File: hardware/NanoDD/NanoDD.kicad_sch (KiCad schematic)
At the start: 33 parts, among them J1 Screw_Terminal_01x02, J2 Conn_01x06, J3 Screw_Terminal_01x02, Q1 AO3401A, Q2 AO3401A, U1 MSP430G2452IRSA16, U3 ZD24C128A-XGMB, U4 XC6206PxxxMR, U5 MS5607-02BA

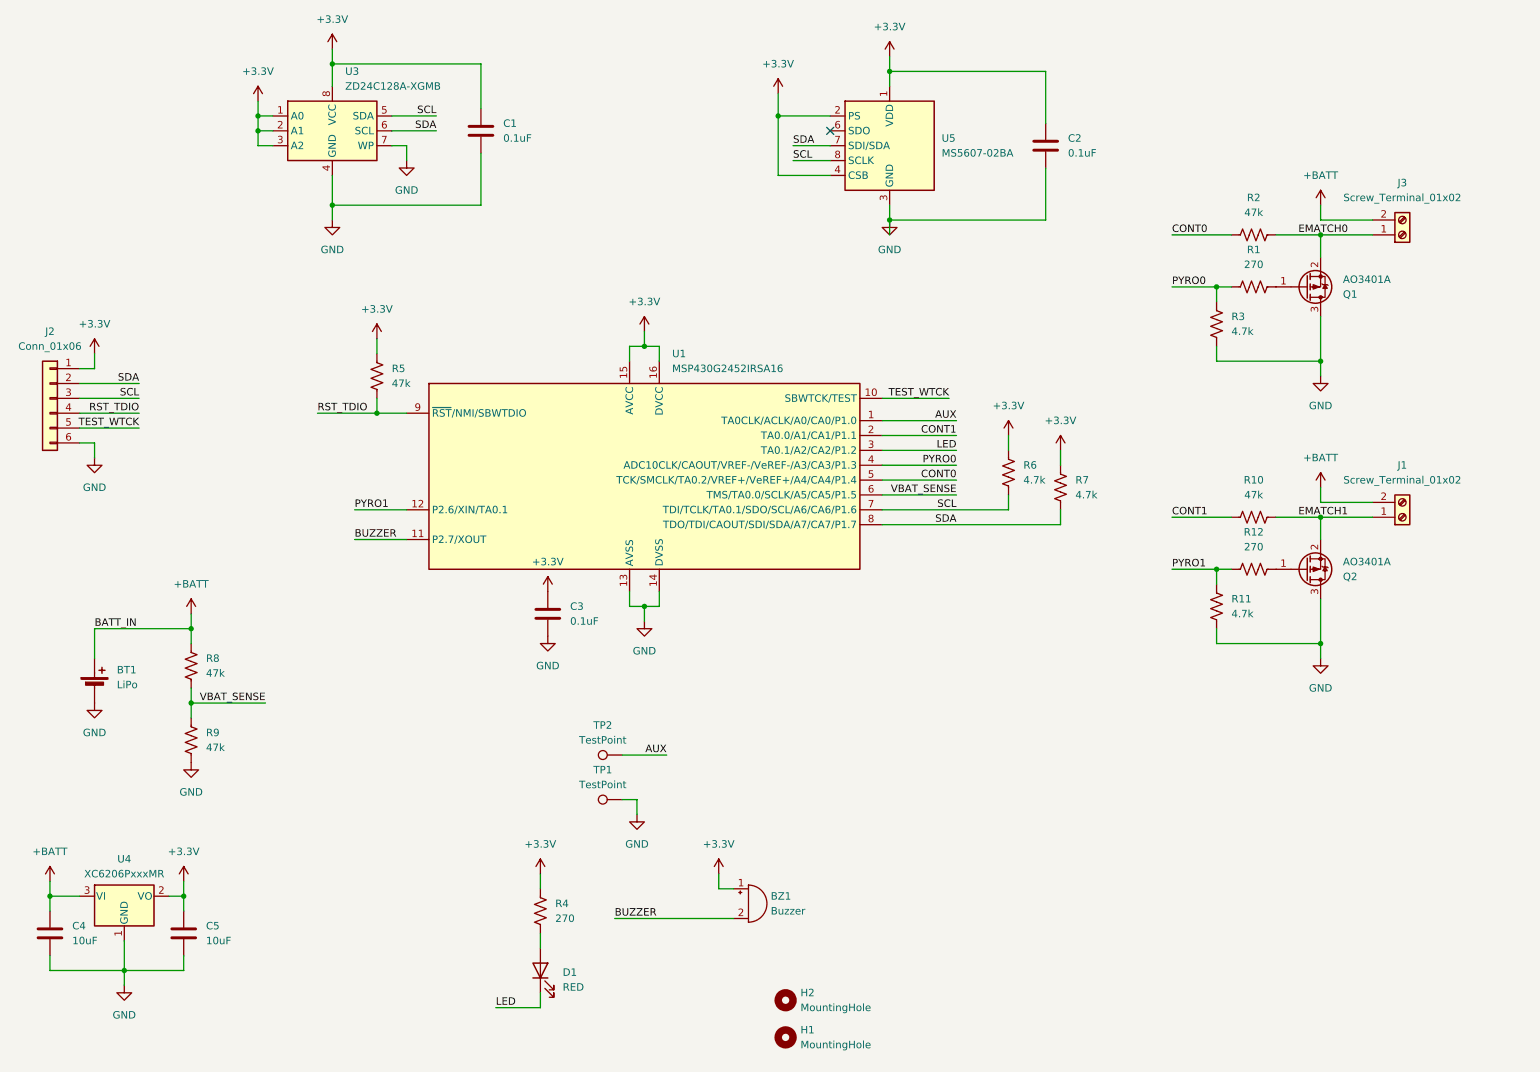
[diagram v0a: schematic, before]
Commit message: Even more layout shrink, switch to barometer that's cheap on JLCPCB
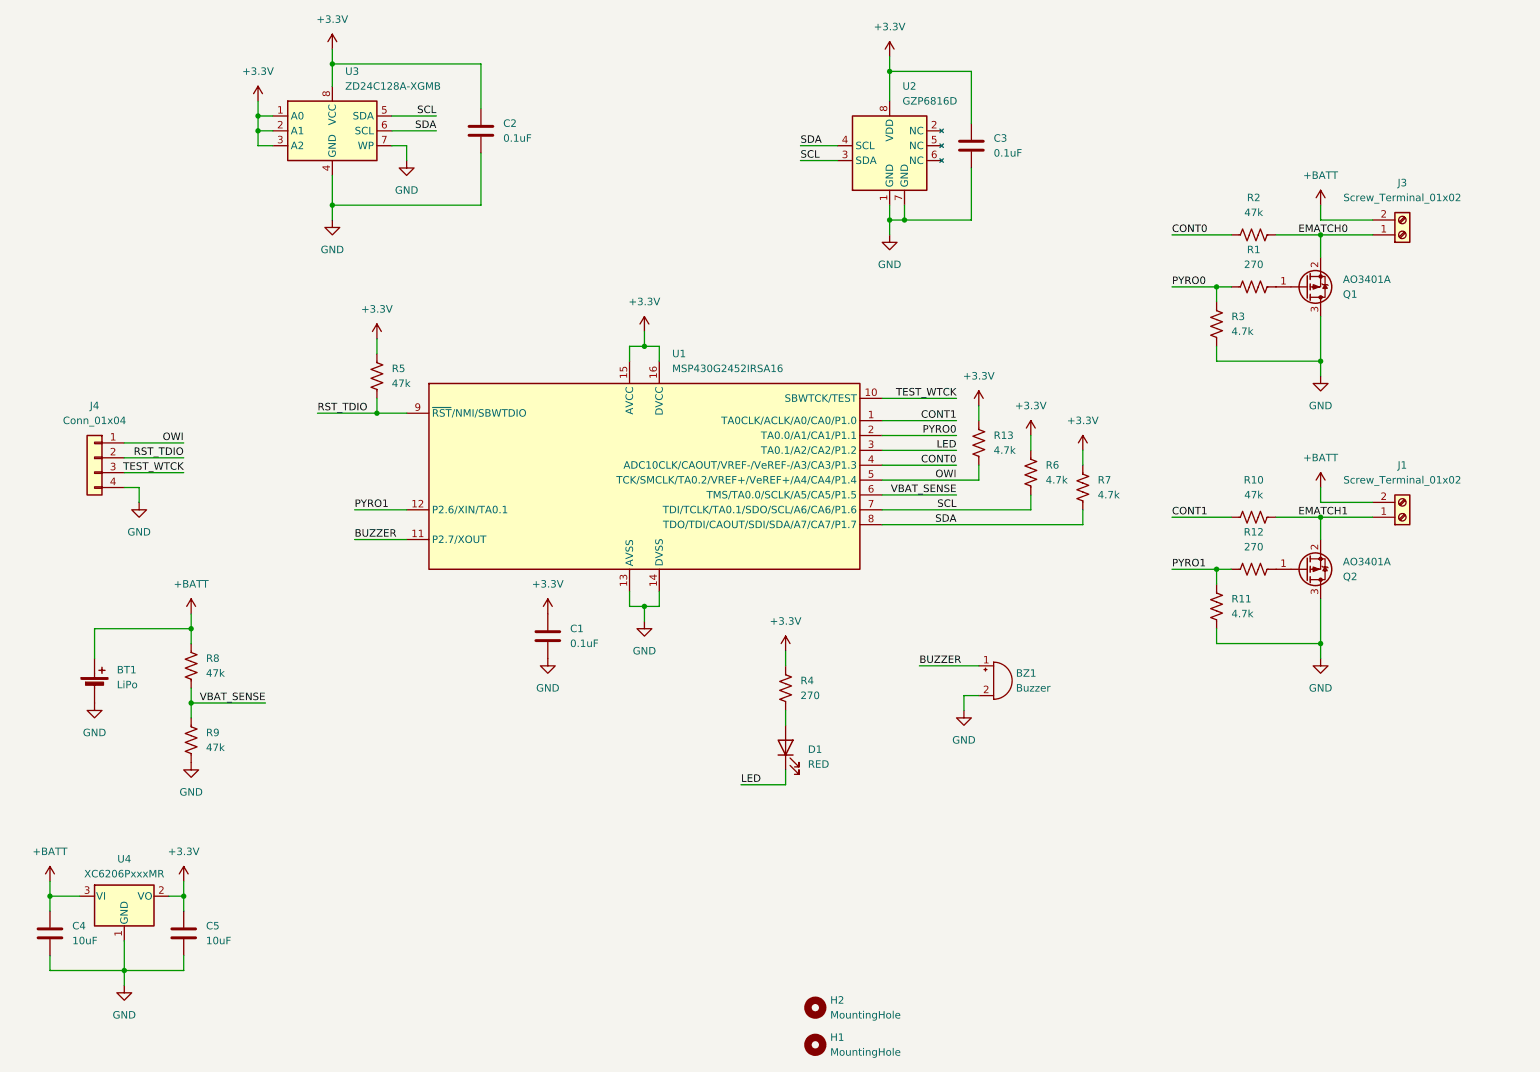
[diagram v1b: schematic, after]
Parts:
- removed J2: Conn_01x06, Connector_Molex:Molex_PicoBlade_53047-0610_1x06_P1.25mm_Vertical, symbol Connector_Generic:Conn_01x06
- removed TP1, TP2: TestPoint, TestPoint:TestPoint_Pad_1.5x1.5mm, symbol Connector:TestPoint
- removed U5: MS5607-02BA, Package_LGA:LGA-8_3x5mm_P1.25mm, symbol Sensor_Pressure:MS5607-02BA
- added J4: Conn_01x04, Connector_Molex:Molex_PicoBlade_53047-0410_1x04_P1.25mm_Vertical, symbol Connector_Generic:Conn_01x04
- added R13: 4.7k, Resistor_SMD:R_0402_1005Metric, symbol Device:R_US
- added U2: GZP6816D, Package_LGA:Bosch_LGA-8_2x2.5mm_P0.65mm_ClockwisePinNumbering, symbol Sensor_Pressure_Custom:GZP6816D
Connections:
- net AUX is gone; now on net CONT1: U1.1 (TA0CLK/ACLK/A0/CA0/P1.0)
- net +3.3V: now also R13.1, U2.8 (VDD); no longer BZ1.1 (+)
- net BUZZER: now also BZ1.1 (+); no longer BZ1.2 (-)
- net CONT0: now also U1.4 (ADC10CLK/CAOUT/VREF-/VeREF-/A3/CA3/P1.3); no longer U1.5 (TCK/SMCLK/TA0.2/VREF+/VeREF+/A4/CA4/P1.4)
- net CONT1: no longer U1.2 (TA0.0/A1/CA1/P1.1)
- net GND: now also BZ1.2 (-), J4.4 (Pin_4), U2.1 (GND), U2.7 (GND)
- net PYRO0: now also U1.2 (TA0.0/A1/CA1/P1.1); no longer U1.4 (ADC10CLK/CAOUT/VREF-/VeREF-/A3/CA3/P1.3)
- net RST_TDIO: now also J4.2 (Pin_2)
- net SCL: now also U2.3 (SDA)
- net SDA: now also U2.4 (SCL)
- net TEST_WTCK: now also J4.3 (Pin_3)
- new net OWI: J4.1 (Pin_1), R13.2, U1.5 (TCK/SMCLK/TA0.2/VREF+/VeREF+/A4/CA4/P1.4)
- no-connect marks 1 -> 0
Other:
- moved on the sheet: BZ1, D1, H1, H2, R4, R6, R7

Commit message: Fixed swapped SCL/SDA
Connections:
- net SCL: now also U2.4 (SCL), U3.6 (SCL); no longer U2.3 (SDA), U3.5 (SDA)
- net SDA: now also U2.3 (SDA), U3.5 (SDA); no longer U2.4 (SCL), U3.6 (SCL)
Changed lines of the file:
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@@
+		)
+	)
+	(label "SCL"
+		(at 154.94 38.1 0)
+		(fields_autoplaced yes)
+		(effects
+			(font
+				(size 1.27 1.27)
+			)
+			(justify left bottom)
 		)
 	)
@@
 		)
 	)
+	(label "SCL"
+		(at 92.71 35.56 180)
+		(fields_autoplaced yes)
+		(effects
+			(font
+				(size 1.27 1.27)
+			)
+			(justify right bottom)
+		)
+	)
 	(label "BUZZER"
 		(at 78.74 105.41 0)
@@
 		)
 	)
-	(label "SCL"
-		(at 92.71 33.02 180)
-		(fields_autoplaced yes)
-		(effects
-			(font
-				(size 1.27 1.27)
-			)
-			(justify right bottom)
-		)
-	)
 	(label "VBAT_SENSE"
 		(at 181.61 97.79 180)
@@
 		)
 	)
+	(label "SDA"
+		(at 92.71 33.02 180)
+		(fields_autoplaced yes)
+		(effects
+			(font
+				(size 1.27 1.27)
+			)
+			(justify right bottom)
+		)
+	)
+	(label "SDA"
+		(at 154.94 40.64 0)
+		(fields_autoplaced yes)
+		(effects
+			(font
+				(size 1.27 1.27)
+			)
+			(justify left bottom)
+		)
+	)
 	(label "PYRO0"
 		(at 181.61 87.63 180)
@@
 		)
 	)
-	(label "SDA"
-		(at 92.71 35.56 180)
-		(fields_autoplaced yes)
-		(effects
-			(font
-				(size 1.27 1.27)
-			)
-			(justify right bottom)
-		)
-	)
 	(label "VBAT_SENSE"
 		(at 63.5 133.35 180)
@@
 		)
 	)
-	(label "SCL"
-		(at 154.94 40.64 0)
-		(fields_autoplaced yes)
-		(effects
-			(font
-				(size 1.27 1.27)
-			)
-			(justify left bottom)
-		)
-	)
 	(label "CONT0"
 		(at 181.61 92.71 180)
@@
 		(fields_autoplaced yes)
 		(effects
-			(font
-				(size 1.27 1.27)
-			)
-			(justify left bottom)
-		)
-	)
-	(label "SDA"
-		(at 154.94 38.1 0)
-		(fields_autoplaced yes)
-		(effects

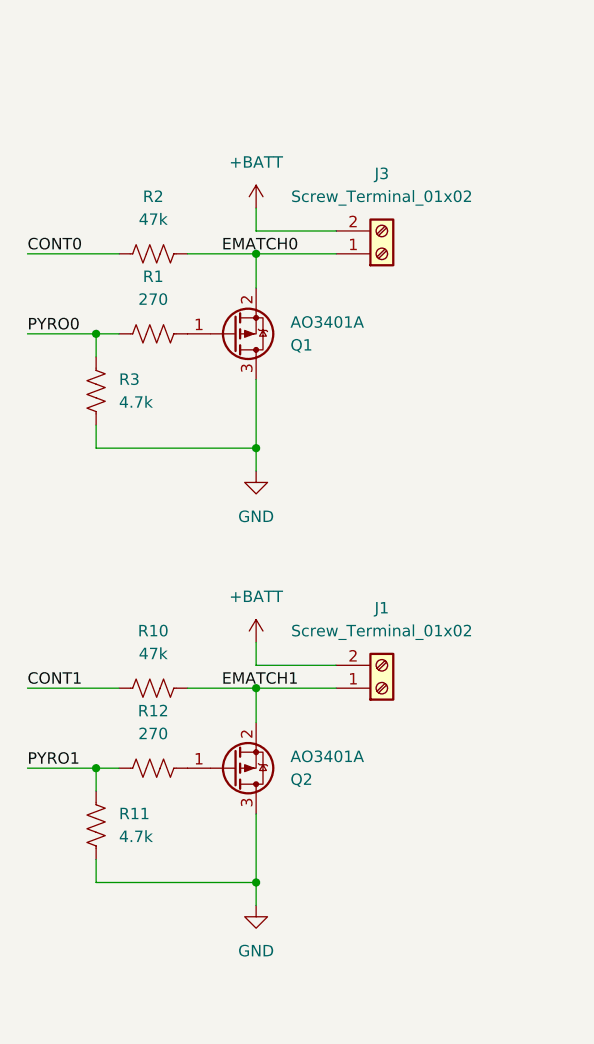
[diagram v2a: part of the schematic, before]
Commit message: Correct MOSFETs and slightly better routing
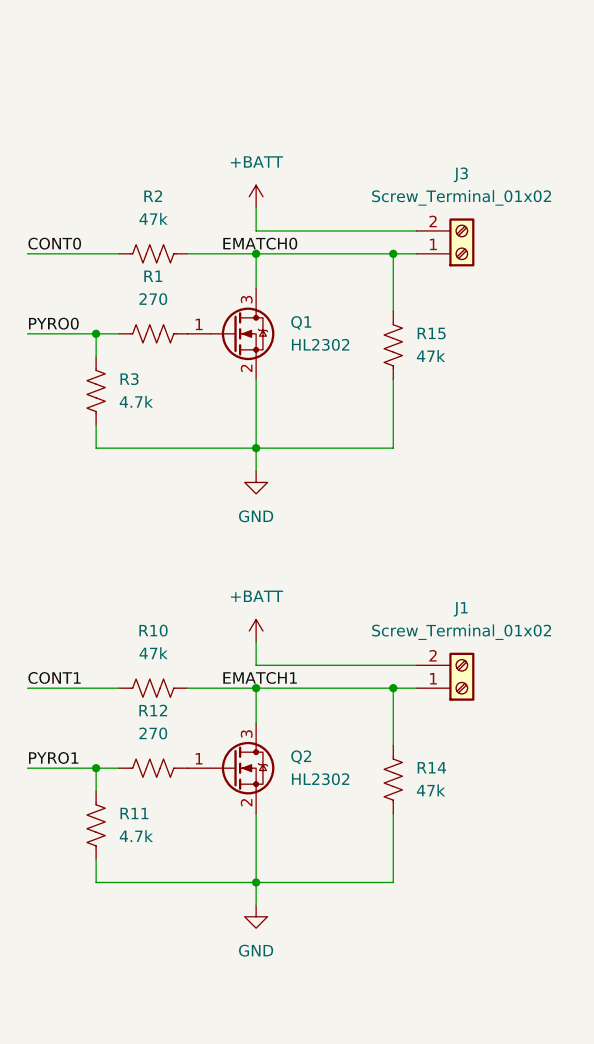
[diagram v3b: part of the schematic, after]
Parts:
- removed Q1, Q2: AO3401A, Package_TO_SOT_SMD:SOT-23, symbol Transistor_FET:AO3401A
- added Q1, Q2: HL2302, Package_TO_SOT_SMD:SOT-23, symbol Device:Q_NMOS_GSD
- added R14, R15: 47k, Resistor_SMD:R_0402_1005Metric, symbol Device:R_US
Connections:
- net EMATCH0: now also Q1.3 (D), R15.2
- net EMATCH1: now also Q2.3 (D), R14.2
- net GND: now also Q1.2 (S), Q2.2 (S), R14.1, R15.1
- net at R12.1: now also Q2.1 (G)
- net at R1.1: now also Q1.1 (G)
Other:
- moved on the sheet: J1, J3

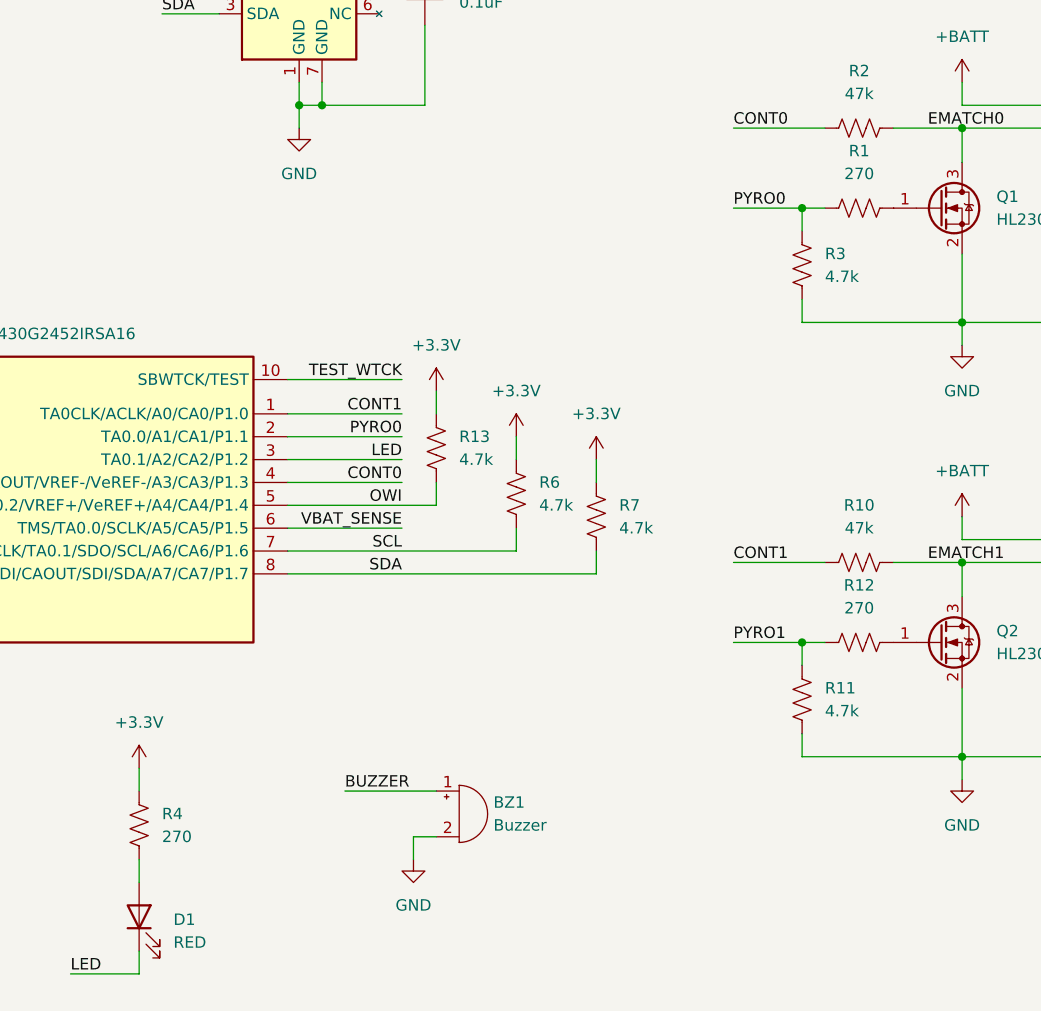
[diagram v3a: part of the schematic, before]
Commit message: Ported to msp430-gcc because CCS on linux is bad
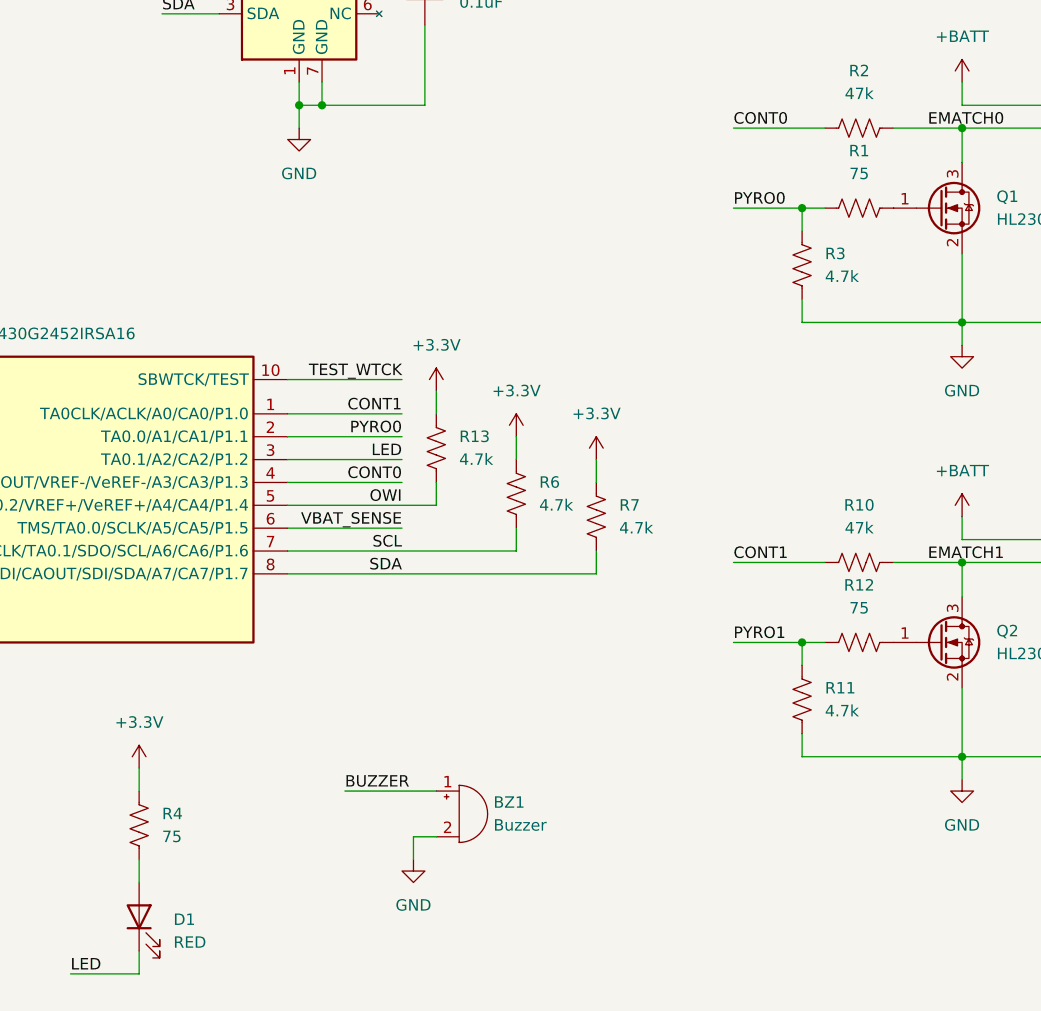
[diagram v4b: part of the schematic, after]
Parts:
- Q1, Q2: JLCPCB_CORRECTION (none) -> 0;0;90; LCSC (none) -> C28646268
- R1, R12, R4: value 270 -> 75; LCSC C25155 -> C25133
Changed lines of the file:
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@@
 			)
 		)
-		(property "Value" "270"
+		(property "Value" "75"
 			(at 232.41 58.42 90)
 			(effects
@@
 			)
 		)
-		(property "LCSC" "C25155"
+		(property "LCSC" "C25133"
 			(at 232.41 62.23 0)
 			(effects
@@
 			)
 		)
+		(property "LCSC" "C28646268"
+			(at 241.3 62.23 0)
+			(effects
+				(font
+					(size 1.27 1.27)
+				)
+				(hide yes)
+			)
+		)
+		(property "JLCPCB_CORRECTION" "0;0;90"
+			(at 241.3 62.23 0)
+			(effects
+				(font
+					(size 1.27 1.27)
+				)
+				(hide yes)
+			)
+		)
 		(pin "3"
 		)
@@
 			)
 		)
-		(property "Value" "270"
+		(property "Value" "75"
 			(at 232.41 106.68 90)
 			(effects
@@
 			)
 		)
-		(property "LCSC" "C25155"
+		(property "LCSC" "C25133"
 			(at 232.41 110.49 0)
 			(effects
@@
 		)
 		(property "Description" "N-MOSFET transistor, gate/source/drain"
+			(at 241.3 110.49 0)
+			(effects
+				(font
+					(size 1.27 1.27)
+				)
+				(hide yes)
+			)
+		)
+		(property "LCSC" "C28646268"
+			(at 241.3 110.49 0)
+			(effects
+				(font
+					(size 1.27 1.27)
+				)
+				(hide yes)
+			)
+		)
+		(property "JLCPCB_CORRECTION" "0;0;90"
 			(at 241.3 110.49 0)
 			(effects
@@
 		(fields_autoplaced yes)
 		(property "Reference" "R4"
-			(at 154.94 129.54 0)
+			(at 154.94 129.5399 0)
 			(effects
 				(font
@@
 			)
 		)
-		(property "Value" "270"
-			(at 154.94 132.08 0)
+		(property "Value" "75"
+			(at 154.94 132.0799 0)
 			(effects
 				(font
@@
 			)
 		)
-		(property "LCSC" "C25155"
+		(property "LCSC" "C25133"
 			(at 152.4 130.81 0)
 			(effects
